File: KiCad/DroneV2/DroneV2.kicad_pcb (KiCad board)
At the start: 2 copper layers, 70 x 70 mm, 15 parts, among them U1 GY-80, U2 ARDUINO_MICRO_SHIELD, U3 LM7809CT, U4 Battery_Connector

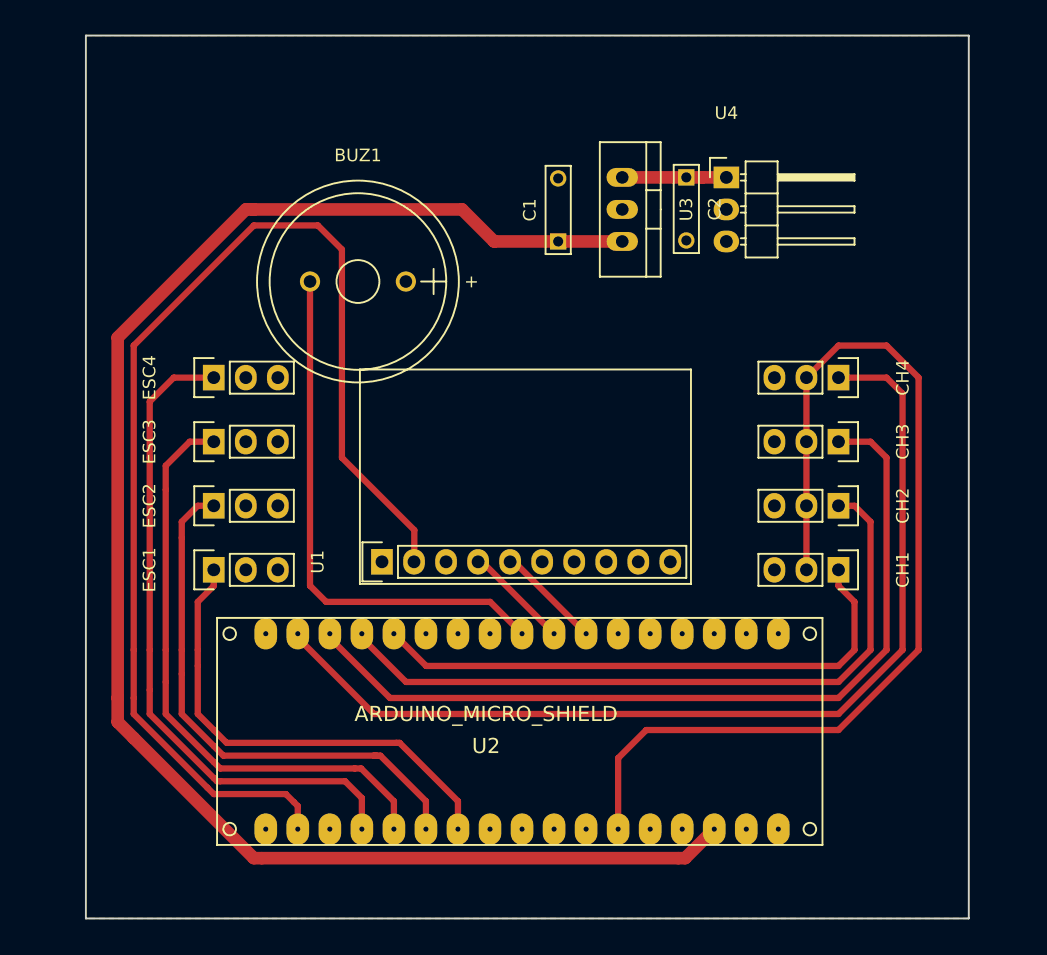
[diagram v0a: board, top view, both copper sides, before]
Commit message: Changing pads width and track's layer
Tracks are now on the bottom copper layer.
Pads are wider (oval) with a smaller hole in the middle
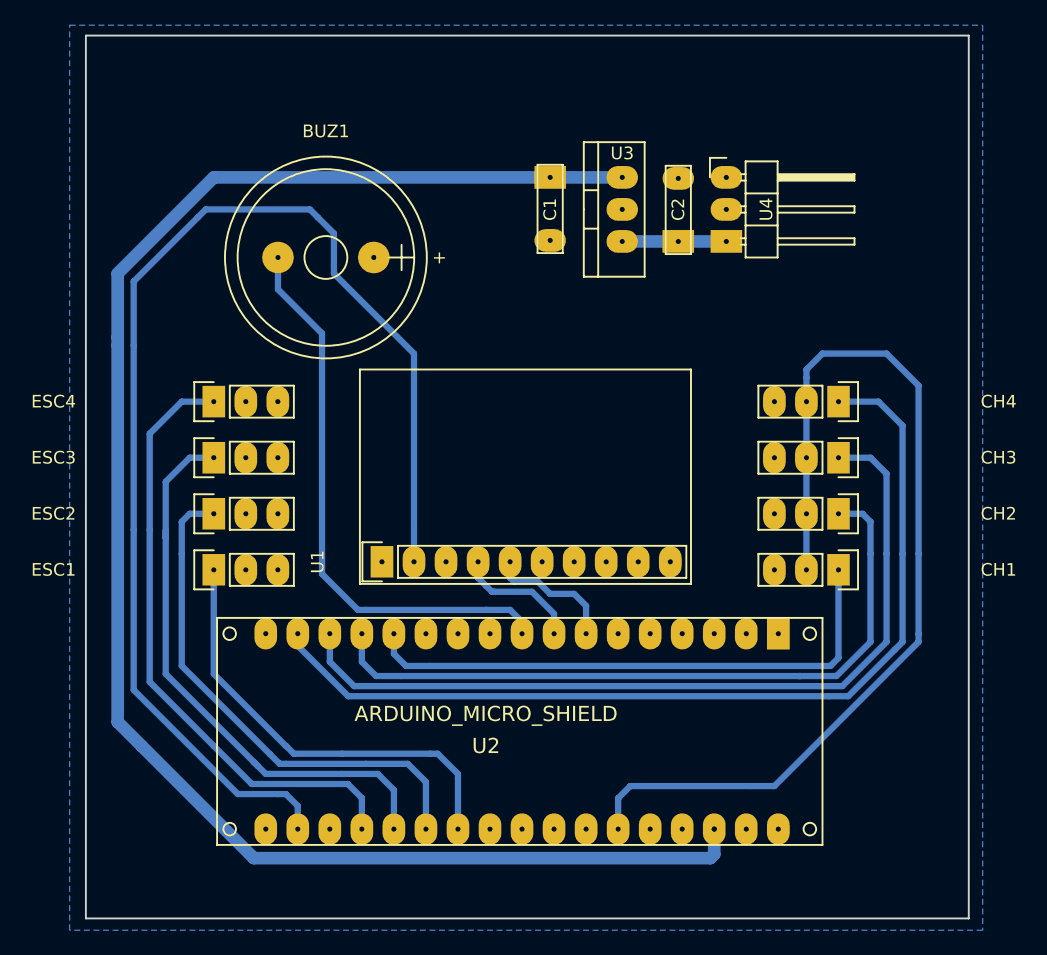
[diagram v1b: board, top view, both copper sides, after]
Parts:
- BUZ1: footprint Buzzers_Beepers:MagneticBuzzer_StarMicronics_HMB-06_HMB-12 -> drone-custom:MagneticBuzzer_StarMicronics_HMB-06_HMB-12_custom
- C1, C2: footprint Capacitors_ThroughHole:C_Rect_L7_W2_P5 -> drone-custom:C_Rect_L7_W2_P5_custom
- CH1, CH2, CH3, CH4, ESC1, ESC2, ESC3, ESC4: footprint Pin_Headers:Pin_Header_Straight_1x03 -> drone-custom:Pin_Header_Straight_1x03_custom
- U1: footprint GY-80:GY-80-Footprint -> drone-custom:GY-80-Footprint_wider_pad
- U2: footprint arduino_micro_shield:ARDUINO_MICRO_SHIELD -> drone-custom:ARDUINO_MICRO_SHIELD_custom
- U3: footprint TO_SOT_Packages_THT:TO-220_Neutral123_Vertical -> drone-custom:TO-220_Neutral123_Vertical_custom
- U4: footprint Pin_Headers:Pin_Header_Angled_1x03 -> drone-custom:Pin_Header_Angled_1x03_custom
- moved C1 5.12 mm to (130.8, 55.2), turned to 270 degrees
- moved C2 5.12 mm to (141.0, 60.3), turned to 90 degrees
- moved BUZ1 3.18 mm to (109.2, 61.6)
- moved CH4 1.91 mm to (153.7, 73.0)
- moved ESC4 1.91 mm to (104.1, 73.0)
- moved CH3 1.27 mm to (153.7, 77.5)
- moved ESC3 1.27 mm to (104.1, 77.5)
- moved CH2 0.64 mm to (153.7, 81.9)
- moved ESC2 0.64 mm to (104.1, 81.9)
- turned U3 to 90 degrees
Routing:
- net Net-(C1-Pad1): track 128.6 -> 133.3 mm, vias 0 -> 1
- net Net-(ESC4-Pad1): track 52.7 -> 48.9 mm
- net /ARDUINO_3.3V: track 95.5 -> 98.7 mm
- net Net-(CH4-Pad1): track 78.8 -> 75.7 mm
- net Net-(ESC1-Pad1): track 38.2 -> 35.3 mm
- net +5V: track 80.8 -> 78.1 mm
- net Net-(BUZ1-Pad1): track 42.5 -> 44.9 mm
- net Net-(U1-Pad5): track 8.35 -> 10.8 mm
- net Net-(U1-Pad4): track 8.35 -> 10.4 mm
- net Net-(ESC2-Pad1): track 43.0 -> 41.1 mm
- net Net-(ESC3-Pad1): track 47.4 -> 45.9 mm
- net Net-(CH3-Pad1): track 67.9 -> 66.9 mm
- net Net-(CH2-Pad1): track 56.4 -> 57.0 mm
- added copper zone on B.Cu, net GND
- removed copper zone on F.Cu, net GND
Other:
- net class 0.5 mm: clearance 0.25 -> 0.3
- net class 1 mm: clearance 0.25 -> 0.3

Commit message: Mise à jour PCB
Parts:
- moved U2 0.64 mm to (152.4, 90.8)
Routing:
- net Net-(CH4-Pad1): track 75.7 -> 77.9 mm
- net /ARDUINO_3.3V: track 98.7 -> 100.4 mm
- net +5V: track 78.1 -> 76.8 mm
- net Net-(U1-Pad5): track 10.8 -> 10.2 mm
- net Net-(CH3-Pad1): track 66.9 -> 67.5 mm
- net Net-(CH1-Pad1): track 44.8 -> 45.3 mm
- net Net-(ESC3-Pad1): track 45.9 -> 45.4 mm
- net Net-(C1-Pad1): track 133.3 -> 133.6 mm, vias 1 -> 0
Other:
- net class 0.5 mm: trace_width 0.5 -> 0.7
